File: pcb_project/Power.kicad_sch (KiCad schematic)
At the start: 0 parts

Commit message: Create power supply circuit
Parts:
- added C10, C19: 1u, symbol Device:C
- added C11, C13, C4: 10u, symbol Device:C
- added C12, C14, C17, C18, C5, C7: 100n, symbol Device:C
- added C15, C16, C20, C21, C8, C9: 22u, symbol Device:C
- added C3: 3.3.n, symbol Device:C
- added C6: 100u, symbol Device:C_Polarized_US
- added FB1: FerriteBead, symbol Device:FerriteBead
- added IC1: TPS54325PWPR, Project_Footprints:SOP65P640X120-15N, symbol TPS54325PWPR:TPS54325PWPR
- added IC2: TPS54294PWPR, symbol TPS54294PWPR:TPS54294PWPR
- added L1, L2: 1.5u, symbol Device:L
- added L3: 2.2u, symbol Device:L
- added R13, R17, R20: 22.1k, symbol Device:R
- added R14: 6.81k, symbol Device:R
- added R15, R18: 100k, symbol Device:R
- added R16: 30.1k, symbol Device:R
- added R19: 73.2k, symbol Device:R
- added R21: 1, symbol Device:R
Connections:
- new net: C7.1, IC1.12 (VBST)
- new net: C7.2, IC1.10 (SW1), IC1.11 (SW2), L1.1
- new net: C17.2, IC2.3 (SW1), L2.1
- new net: C18.2, IC2.14 (SW2), L3.1
- new net: IC2.10 (VFB2), R19.2, R20.1
- new net: C19.1, IC2.9 (VREG5), R18.1
- new net: IC2.12 (EN2), IC2.6 (PG1), R18.2
- new net: C10.1, IC1.3 (VREG5), R15.2
- new net: IC2.7 (VFB1), R16.2, R17.1
- new net: C18.1, IC2.15 (VBST2)
- new net: C17.1, IC2.2 (VBST1)
- new net: IC1.6 (PG), IC2.5 (EN1), R15.1
- new net: FB1.2, R21.1
- new net: IC1.2 (VFB), R13.1, R14.2
- new net: C3.1, IC1.4 (SS)
- new net 1V0: C8.1, C9.1, IC1.1 (VO), L1.2, R13.2
- new net 1V8: C15.1, C16.1, L2.2, R16.1
- new net 3.3VA: R21.2
- new net 3V3: C20.1, C21.1, FB1.1, L3.2, R19.1
- new net GND: C10.2, C11.2, C12.2, C13.2, C14.2, C15.2, C16.2, C19.2, C20.2, C21.2, C3.2, C4.2, C5.2, C6.2, C8.2, C9.2, IC1.15 (EP), IC1.5 (GND), IC1.8 (PGND1), IC1.9 (PGND2), IC2.13 (PGND2), IC2.17 (EP), IC2.4 (PGND1), IC2.8 (GND), R14.1, R17.2, R20.2
- new net POWER_IN: C11.1, C12.1, C13.1, C14.1, C4.1, C5.1, C6.1, IC1.13 (VIN), IC1.14 (VCC), IC1.7 (EN), IC2.1 (VIN1), IC2.16 (VIN2)
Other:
- note added: "1%"
- note added: "4.5V - 18V"
- note added: "lp>2.8A, lrms>2.1A"
- note added: "lp>2.9A, lrms>2.1A"
- note added: "lp>3.5A, lrms>3.1A"

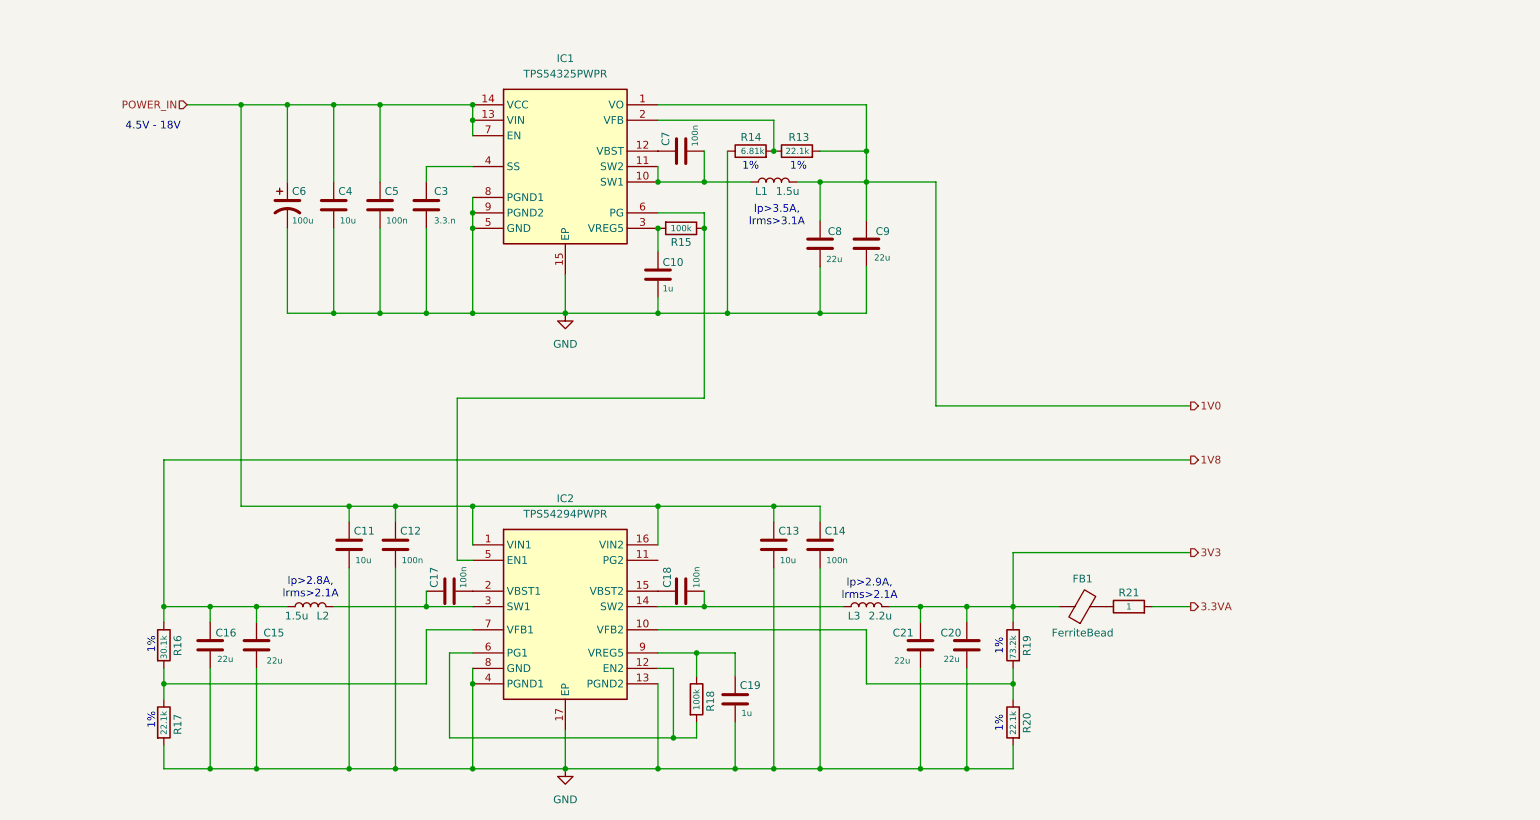
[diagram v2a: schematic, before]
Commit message: Add MicroUSB as power input
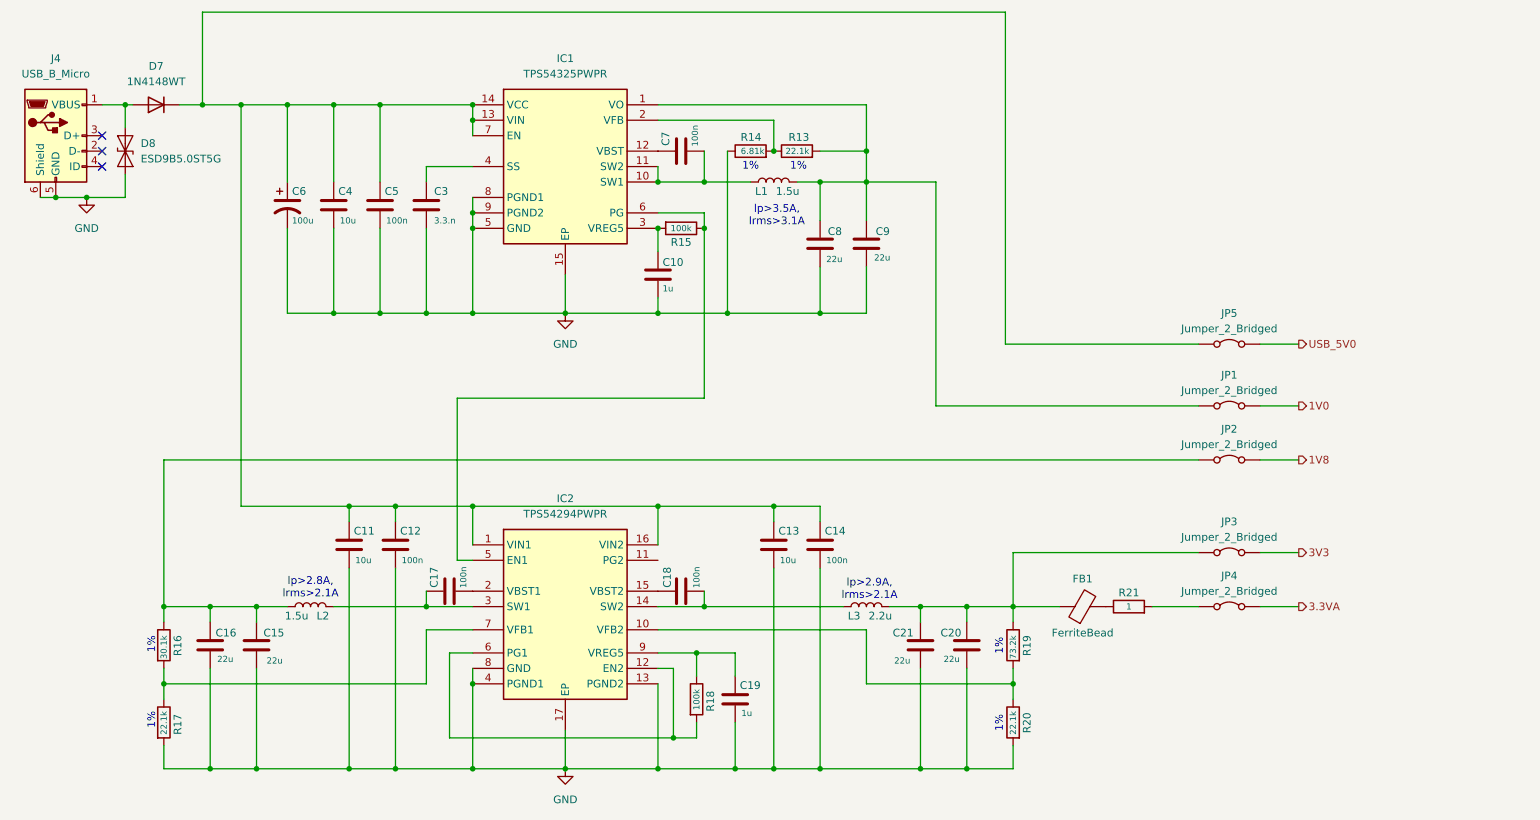
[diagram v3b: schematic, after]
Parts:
- added D7: 1N4148WT, Diode_SMD:D_SOD-523, symbol Diode:1N4148WT
- added D8: ESD9B5.0ST5G, Diode_SMD:D_SOD-923, symbol Diode:ESD9B5.0ST5G
- added J4: USB_B_Micro, symbol Connector:USB_B_Micro
- added JP1, JP2, JP3, JP4, JP5: Jumper_2_Bridged, symbol Jumper:Jumper_2_Bridged
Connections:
- net 1V0: now also JP1.2 (B); no longer C8.1, C9.1, IC1.1 (VO), L1.2, R13.2
- net 1V8: now also JP2.2 (B); no longer C15.1, C16.1, L2.2, R16.1
- net 3.3VA: now also JP4.2 (B); no longer R21.2
- net 3V3: now also JP3.2 (B); no longer C20.1, C21.1, FB1.1, L3.2, R19.1
- net GND: now also D8.1 (A1), J4.5 (GND), J4.6 (Shield)
- net POWER_IN: no longer names the net of C11.1, C12.1, C13.1, C14.1, C4.1, C5.1, C6.1, IC1.13 (VIN), IC1.14 (VCC), IC1.7 (EN), IC2.1 (VIN1), IC2.16 (VIN2)
- net POWER_IN: now also D7.1 (K), JP5.1 (A)
- new net: D7.2 (A), D8.2 (A2), J4.1 (VBUS)
- new net: C15.1, C16.1, JP2.1 (A), L2.2, R16.1
- new net: C20.1, C21.1, FB1.1, JP3.1 (A), L3.2, R19.1
- new net: C8.1, C9.1, IC1.1 (VO), JP1.1 (A), L1.2, R13.2
- new net: JP4.1 (A), R21.2
- new net USB_5V0: JP5.2 (B)
- no-connect marks 0 -> 3
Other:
- note removed: "4.5V - 18V"

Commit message: Update USB circuits
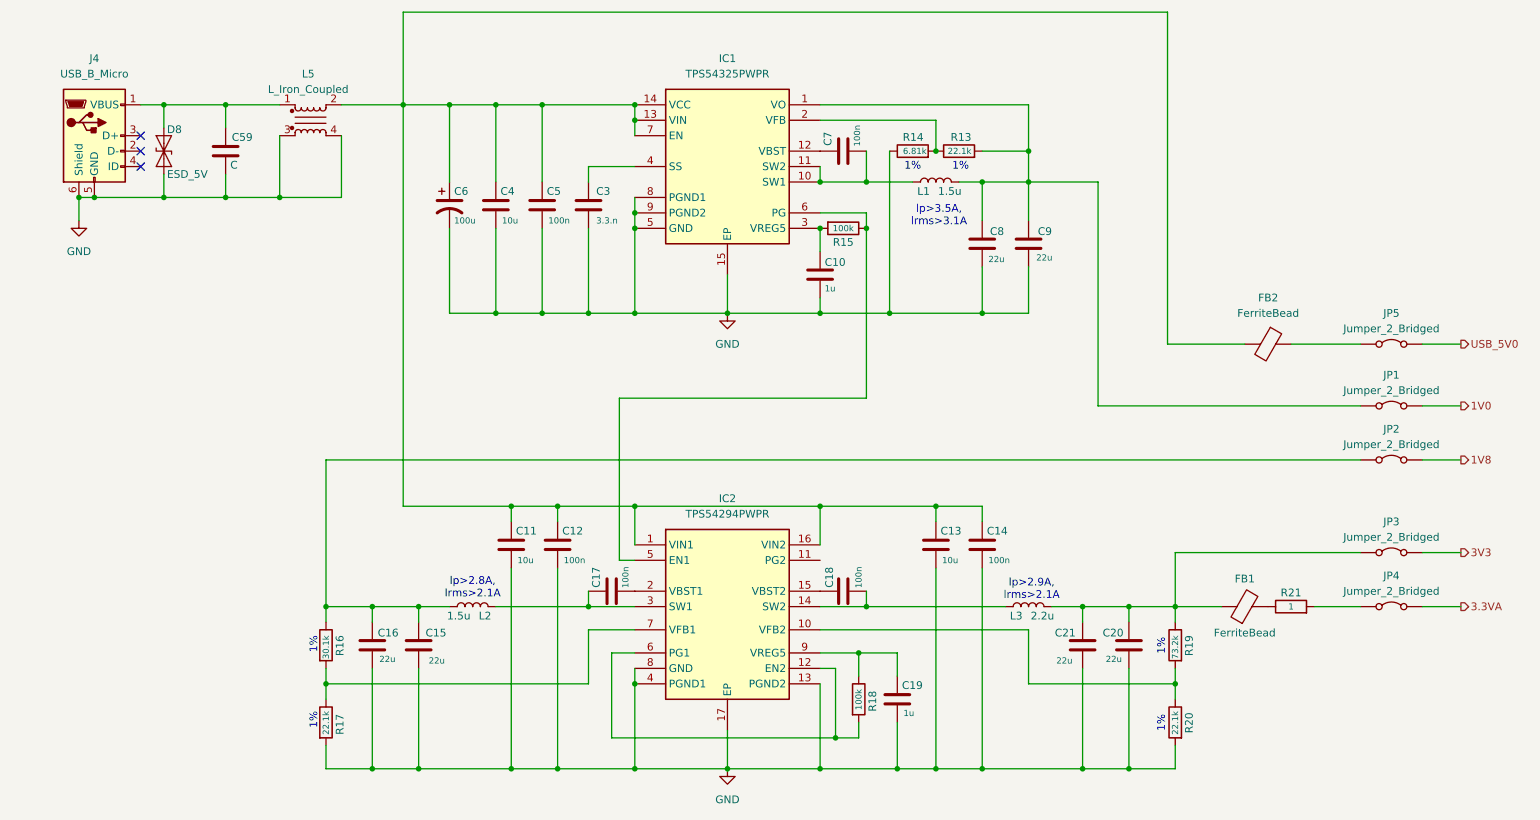
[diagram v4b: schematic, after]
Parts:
- removed D7: 1N4148WT, Diode_SMD:D_SOD-523, symbol Diode:1N4148WT
- added C59: C, symbol Device:C
- added FB2: FerriteBead, symbol Device:FerriteBead
- added L5: L_Iron_Coupled, symbol Device:L_Iron_Coupled
- D8: value ESD9B5.0ST5G -> ESD_5V
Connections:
- net GND: now also C59.2, L5.3, L5.4
- net at D8.2 (A2), J4.1 (VBUS): now also C59.1, L5.1
- net at C11.1, C12.1, C13.1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: now also FB2.2, L5.2; no longer JP5.1 (A)
- new net: FB2.1, JP5.1 (A)
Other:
- moved on the sheet: C10, C11, C12, C13, C14, C15, C16, C17, C18, C19, C20, C21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

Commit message: ERC fixes, some remain
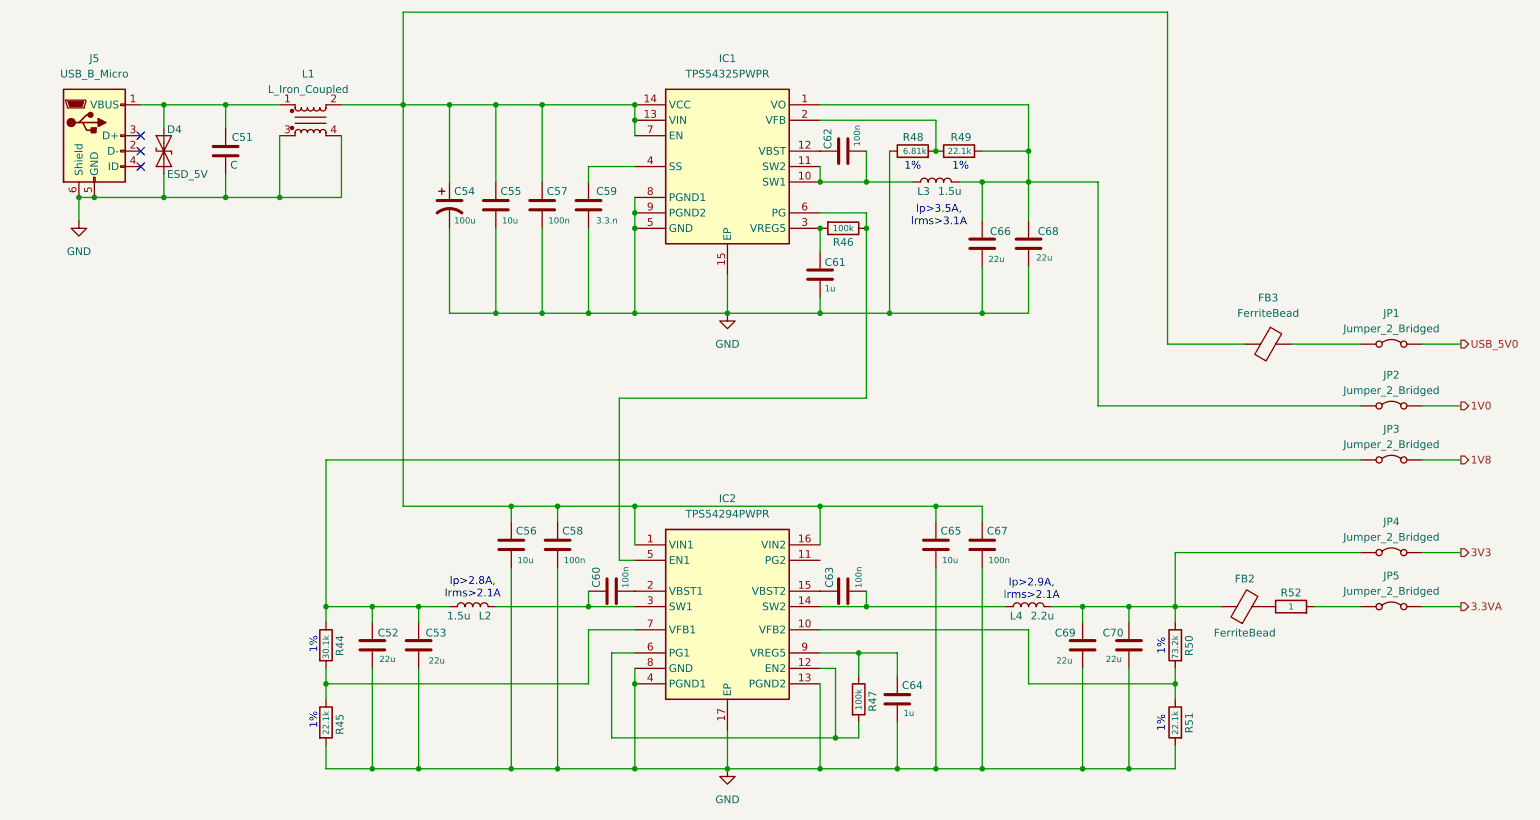
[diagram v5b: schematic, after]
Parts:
- renumbered C59 to C51, C16 to C52, C15 to C53, C6 to C54, C4 to C55, C11 to C56, C5 to C57, C12 to C58, C3 to C59, C17 to C60, C10 to C61, C7 to C62, C18 to C63, C19 to C64, C13 to C65, C8 to C66, C14 to C67, C9 to C68, C21 to C69, C20 to C70, D8 to D4, FB1 to FB2, FB2 to FB3, J4 to J5, JP5 to JP1, JP1 to JP2, JP2 to JP3, JP3 to JP4, JP4 to JP5, L5 to L1, L1 to L3, L3 to L4, R16 to R44, R17 to R45, R15 to R46, R18 to R47, R14 to R48, R13 to R49, R19 to R50, R20 to R51, R21 to R52

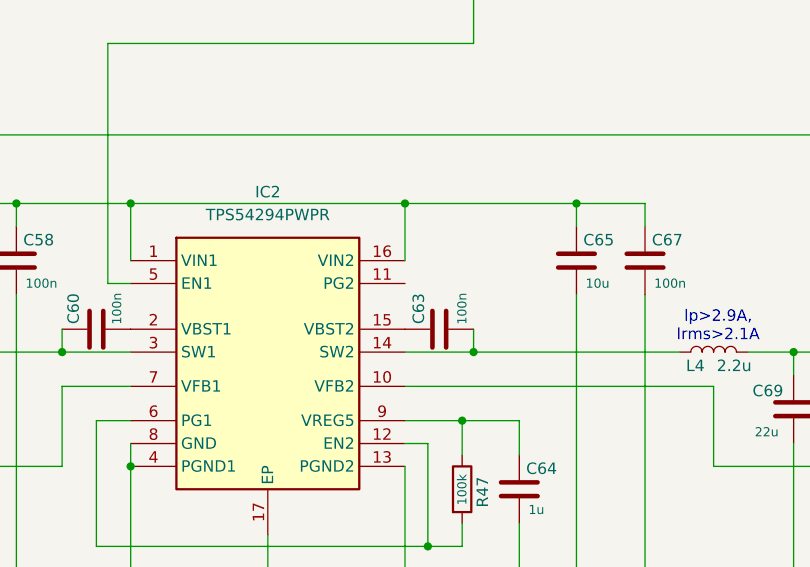
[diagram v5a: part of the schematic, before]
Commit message: Fix USB pins and other ERC errors
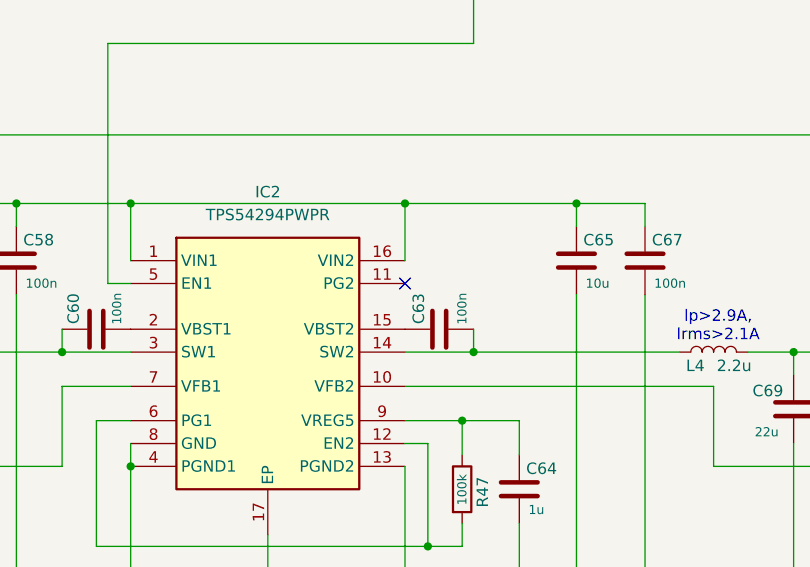
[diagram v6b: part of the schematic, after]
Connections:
- no-connect marks 3 -> 4
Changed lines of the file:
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@@
 		(at 46.99 43.18)
+	)
+	(no_connect
+		(at 158.75 110.49)
 	)
 	(wire
